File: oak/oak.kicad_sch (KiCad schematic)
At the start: 99 parts, among them J13 Conn_02x05_Odd_Even, J14 Conn_01x03, J15 Conn_01x03, J16 AudioJack2, J17 AudioJack2, J18 AudioJack2, J19 Conn_01x02, J21 AudioJack2, J22 AudioJack2, J23 AudioJack2, J24 USB_C_Receptacle_USB2.0_16P, Q10 MMBT3904, Q11 MMBT3904, Q12 MMBT3904, Q13 MMBT3904, Q14 MMBT3904, Q15 MMBT3904, Q16 MMBT3904, Q17 MMBT3904, Q18 MMBT3904, Q19 MMBT3904, Q20 MMBT3904, SW10 SW_MEC_5E, SW11 SW_MEC_5E, SW12 SW_Push, SW6 LP4OA1PBCT, SW7 LP4OA1PBCT, SW8 LP4OA1PBCT, SW9 LP4OA1PBCT, U13 74AHCT1G125, U18 74AHCT1G125, U19 74AHCT1G125, U20 NCP1117-3.3_SOT223, U21 W25Q32JVSS, U22 RP2040, U23 NCP1117-5.0_SOT223, Y1 ABM8-272-T3

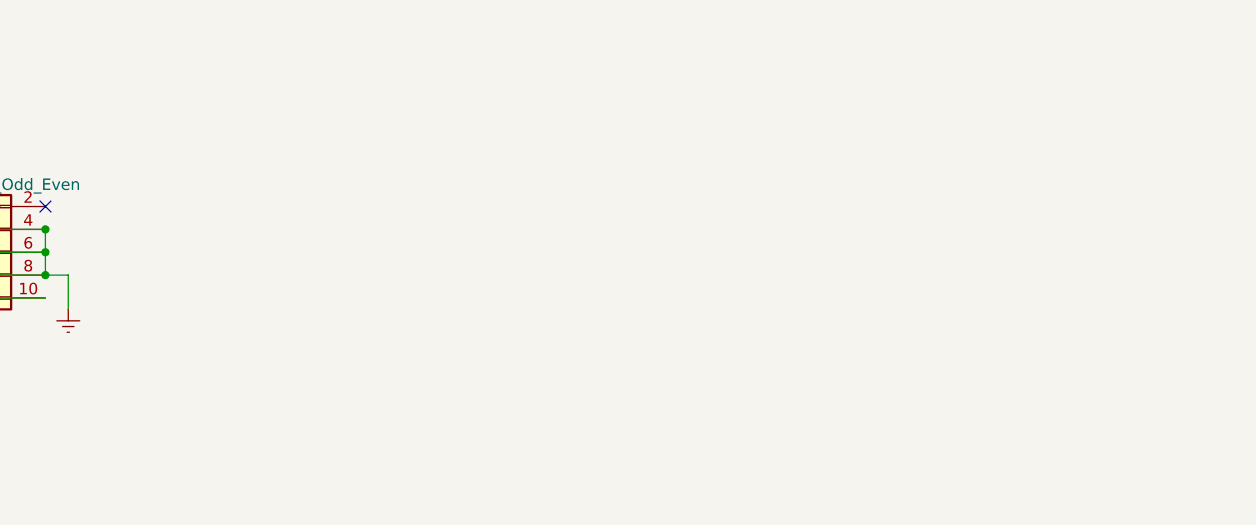
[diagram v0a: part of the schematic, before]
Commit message: Documentation in Oak's schematic
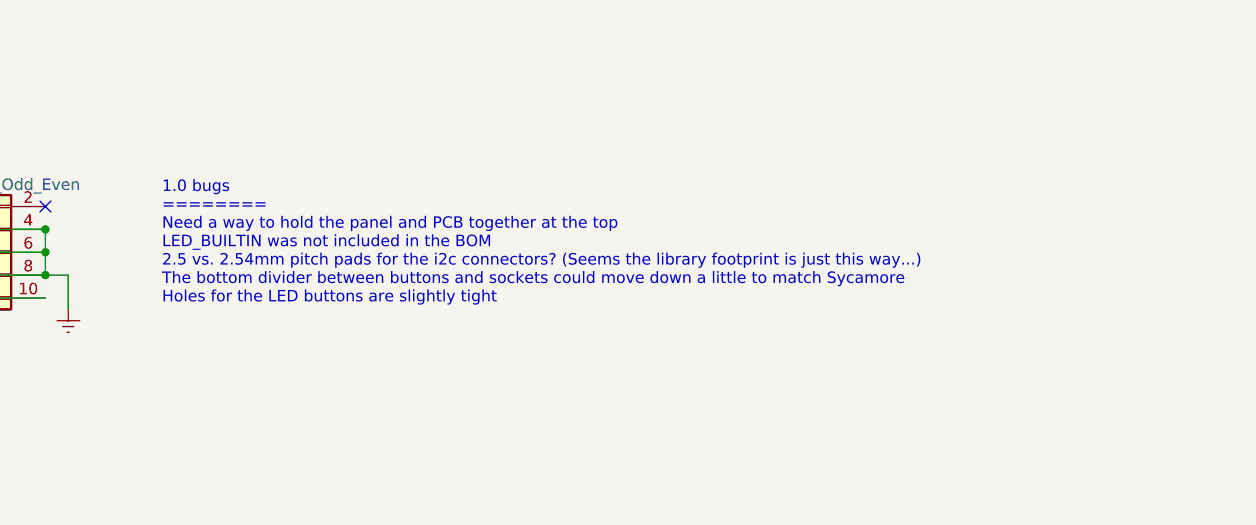
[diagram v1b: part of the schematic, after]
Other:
- note added: "1.0 bugs ======== Need a way to hold the panel and PCB together at the top LED_BUILTIN was not included in the BOM 2.5 vs. 2.54mm pitch pads for the i2c connectors? (Seems the library footprint is just this way...) The bottom divider between buttons and sockets could move down a little to match Sycamore Holes for the LED buttons are slightly tight"

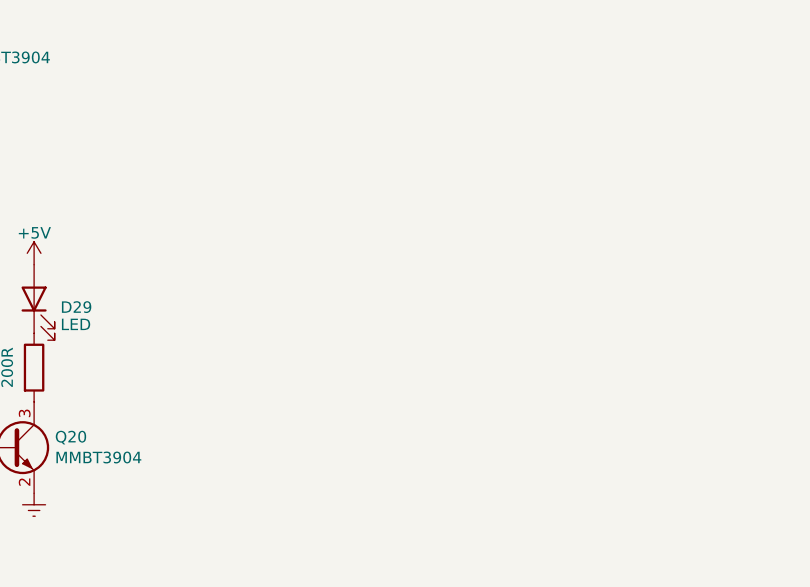
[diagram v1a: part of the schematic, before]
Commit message: Adding Oak BOM, firmware notes, i2c implementation, design files
Missing assembly instructions, and the firmware for Sycamore needs to be updated as well.
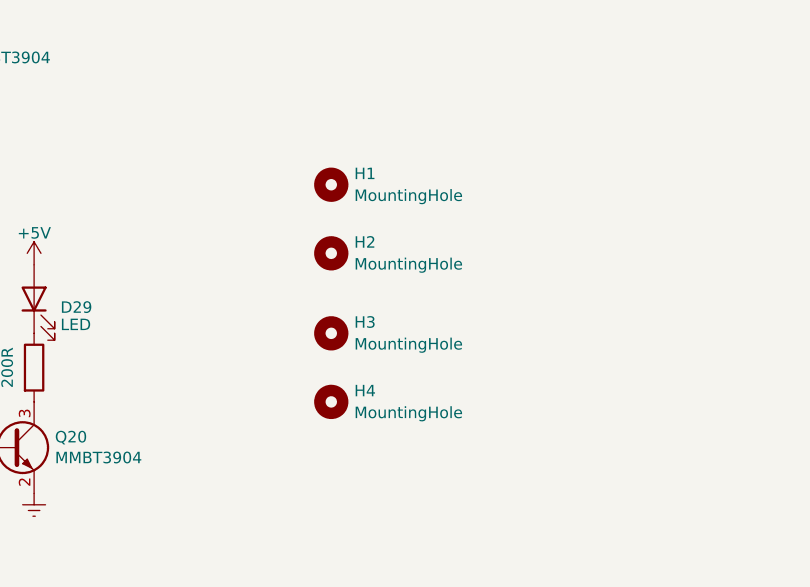
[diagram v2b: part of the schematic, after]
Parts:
- added H1, H2, H3, H4: MountingHole, MountingHole:MountingHole_3mm, symbol Mechanical:MountingHole
